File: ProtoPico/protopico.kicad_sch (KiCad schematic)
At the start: 35 parts, among them J1 Screw_Terminal_01x02, J2 Backpack, J3 Other Fin, J4 BoopSensor, J5 Badger, J6 Face Power, J7 Face Matrices, M1 Fan, U1 Pimoroni_TinyRP2040, U2 Pololu D36V28F5, U3 Pololu D24V10F3, U4 74LS125

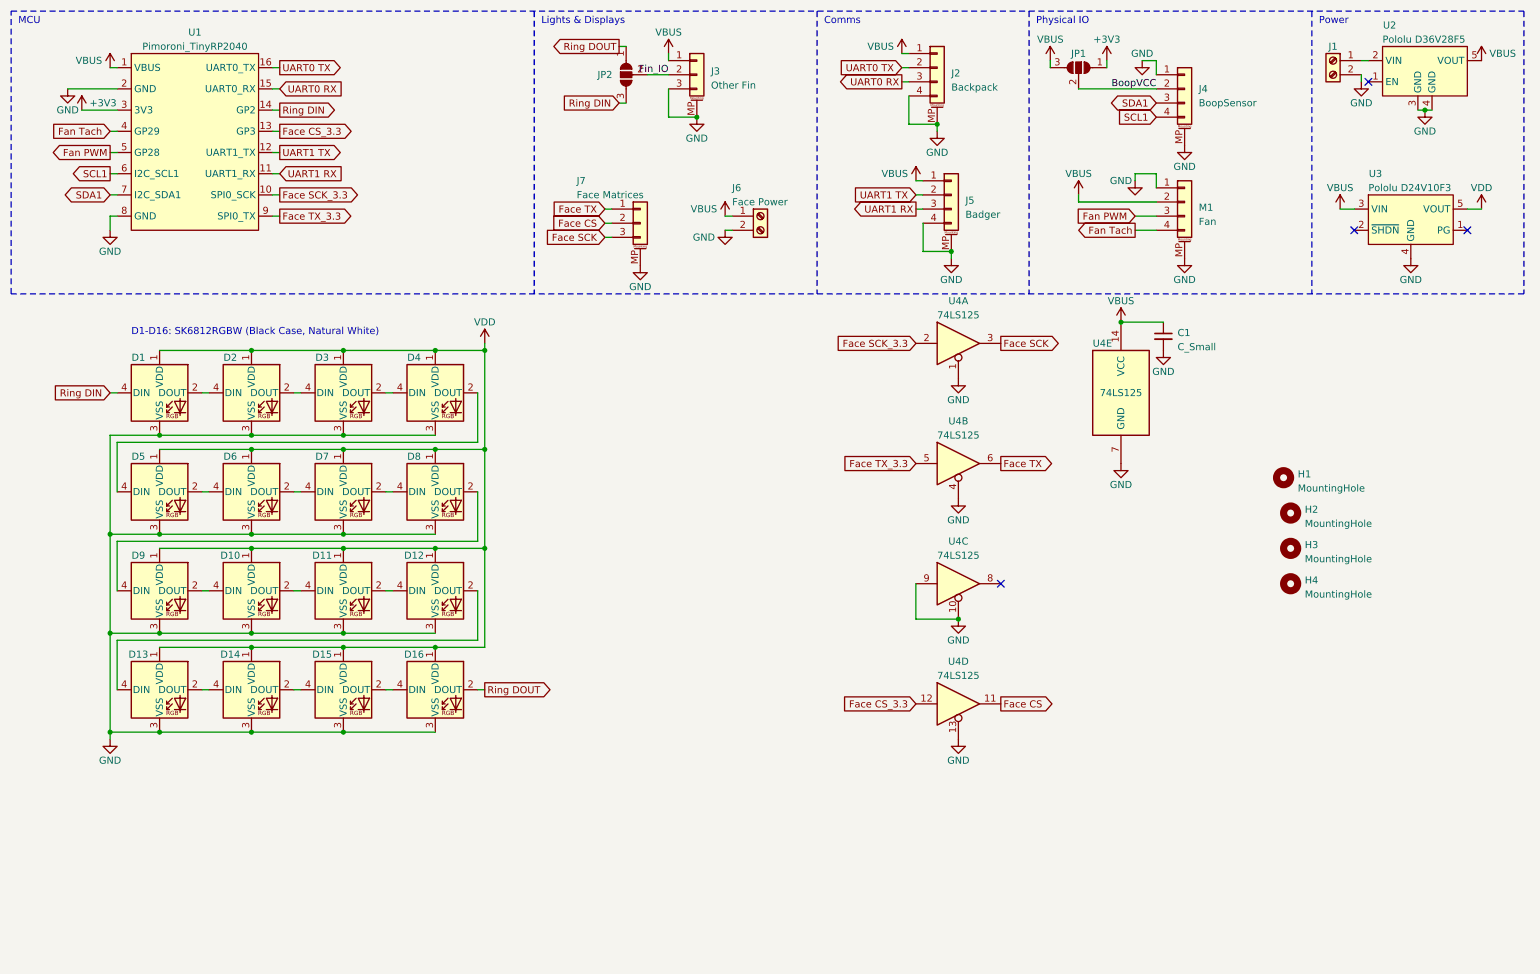
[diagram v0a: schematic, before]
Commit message: Update cheek pcb to Rev 2
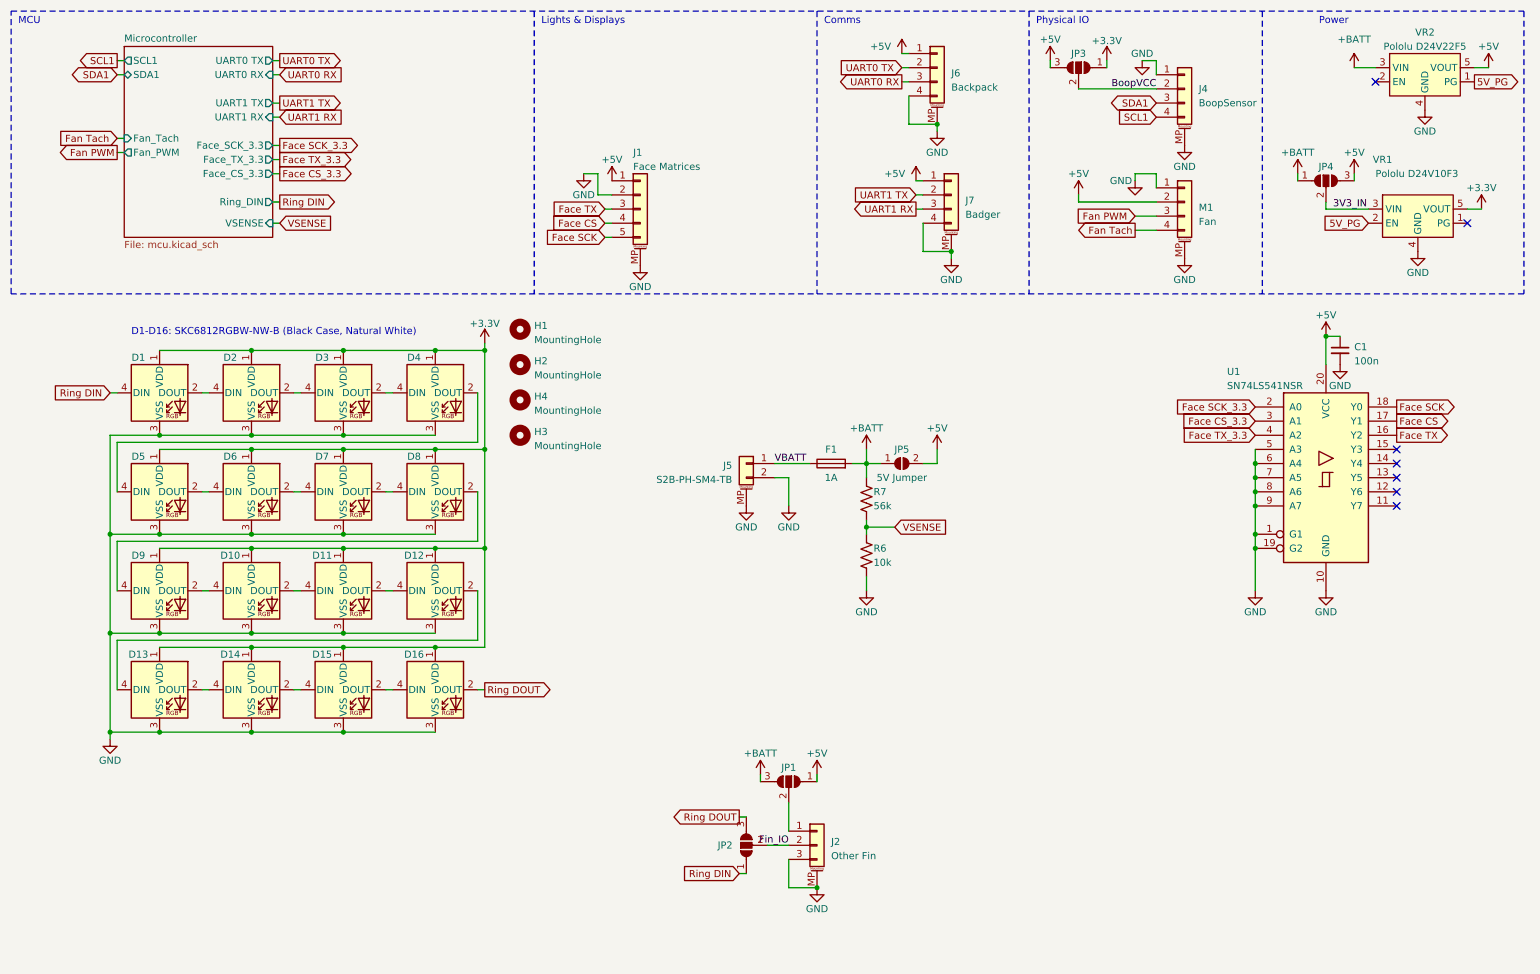
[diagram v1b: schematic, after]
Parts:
- removed J1: Screw_Terminal_01x02, TerminalBlock:TerminalBlock_bornier-2_P5.08mm, symbol Connector:Screw_Terminal_01x02
- removed J3: Other Fin, Connector_JST:JST_PH_S3B-PH-SM4-TB_1x03-1MP_P2.00mm_Horizontal, symbol Connector_Generic_MountingPin:Conn_01x03_MountingPin
- removed J6: Face Power, TerminalBlock:TerminalBlock_bornier-2_P5.08mm, symbol Connector:Screw_Terminal_01x02
- removed J7: Face Matrices, Connector_JST:JST_GH_SM03B-GHS-TB_1x03-1MP_P1.25mm_Horizontal, symbol Connector_Generic_MountingPin:Conn_01x03_MountingPin
- removed U1: Pimoroni_TinyRP2040, MCU_RaspberryPi_and_Boards:Pimoroni_TinyRP2040, symbol MCU_RaspberryPi_and_Boards:Pimoroni_TinyRP2040
- removed U2: Pololu D36V28F5, MyloLibrary:Pololu D36V28Fx, symbol New_Library:Pololu D36V28F5
- removed U4: 74LS125, Package_SO:TSSOP-14_4.4x5mm_P0.65mm, symbol 74xx:74LS125
- added F1: 1A, Fuse:Fuse_1206_3216Metric, symbol Device:Fuse
- added J1: Face Matrices, ProtoPico_Footprints:JST_SH_SM05B-SRSS-TB_1x05-1MP_P1.00mm_Horizontal, symbol Connector_Generic_MountingPin:Conn_01x05_MountingPin
- added J2: Other Fin, Connector_JST:JST_PH_S3B-PH-SM4-TB_1x03-1MP_P2.00mm_Horizontal, symbol Connector_Generic_MountingPin:Conn_01x03_MountingPin
- added J5: S2B-PH-SM4-TB, Connector_JST:JST_PH_S2B-PH-SM4-TB_1x02-1MP_P2.00mm_Horizontal, symbol Connector_Generic_MountingPin:Conn_01x02_MountingPin
- added JP1, JP4: SolderJumper_3_Open, Jumper:SolderJumper-3_P2.0mm_Open_TrianglePad1.0x1.5mm_NumberLabels, symbol Jumper:SolderJumper_3_Open
- added JP5: 5V Jumper, Jumper:SolderJumper-2_P1.3mm_Open_TrianglePad1.0x1.5mm, symbol Jumper:SolderJumper_2_Open
- added R6: 10k, Resistor_SMD:R_0805_2012Metric, symbol Device:R_US
- added R7: 56k, Resistor_SMD:R_0805_2012Metric, symbol Device:R_US
- added U1: SN74LS541NSR, Package_SO:SO-20_5.3x12.6mm_P1.27mm, symbol 74xx:74LS541
- added VR2: Pololu D24V22F5, ProtoPico_Footprints:D24V22FX, symbol ProtoPico_Symbols:D24V22Fx
- C1: value C_Small -> 100n
- D1, D10, D11, D12, D13, D14, D15, D16, D2, D3, D4, D5, D6, D7, D8, D9: value SK6812RGBW -> SKC6812RGBW-NW-B
- J4, M1: footprint Connector_JST:JST_GH_SM04B-GHS-TB_1x04-1MP_P1.25mm_Horizontal -> ProtoPico_Footprints:JST_SH_SM04B-SRSS-TB_1x04-1MP_P1.00mm_Horizontal
- J6: renamed from J2; footprint Connector_JST:JST_GH_SM04B-GHS-TB_1x04-1MP_P1.25mm_Horizontal -> ProtoPico_Footprints:JST_SH_SM04B-SRSS-TB_1x04-1MP_P1.00mm_Horizontal
- J7: renamed from J5; footprint Connector_JST:JST_GH_SM04B-GHS-TB_1x04-1MP_P1.25mm_Horizontal -> ProtoPico_Footprints:JST_SH_SM04B-SRSS-TB_1x04-1MP_P1.00mm_Horizontal
- VR1: renamed from U3; footprint MyloLibrary:Pololu D24V10Fx -> ProtoPico_Footprints:D24V10Fx; symbol New_Library:Pololu D24V10F3 -> ProtoPico_Symbols:D24V10Fx
- renumbered H4 to H3, H3 to H4, JP1 to JP3
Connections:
- net VDD is gone; now on net +3.3V: D1.1 (VDD), D10.1 (VDD), D11.1 (VDD), D12.1 (VDD), D13.1 (VDD), D14.1 (VDD), D15.1 (VDD), D16.1 (VDD), D2.1 (VDD), D3.1 (VDD), D4.1 (VDD), D5.1 (VDD), D6.1 (VDD), D7.1 (VDD), D8.1 (VDD), D9.1 (VDD), VR1.5 (VOUT)
- net Face CS: now also J1.4 (Pin_4), U1.17 (Y1)
- net Face CS_3.3: now also U1.3 (A1)
- net Face SCK: now also J1.5 (Pin_5), U1.18 (Y0)
- net Face SCK_3.3: now also U1.2 (A0)
- net Face TX: now also J1.3 (Pin_3), U1.16 (Y2)
- net Face TX_3.3: now also U1.4 (A2)
- net Fin_IO: now also J2.2 (Pin_2)
- net GND: now also J1.2 (Pin_2), J1.MP (MountPin), J2.3 (Pin_3), J2.MP (MountPin), J5.2 (Pin_2), J5.MP (MountPin), R6.2, U1.1 (G1), U1.10 (GND), U1.19 (G2), U1.5 (A3), U1.6 (A4), U1.7 (A5), U1.8 (A6), U1.9 (A7), VR2.4 (GND), VR2.6 (GND)
- net Ring DIN: now also JP2.1 (A); no longer JP2.3 (B)
- net Ring DOUT: now also JP2.3 (B); no longer JP2.1 (A)
- net 5V_PG: now reaches VR1.2 (EN)
- net 5V_PG: now also VR2.1 (PG)
- net +3V3 renamed +3.3V
- net VBUS renamed +5V
- net +5V: now also J1.1 (Pin_1), JP1.1 (A), JP4.3 (B), JP5.2 (B), U1.20 (VCC), VR2.5 (VOUT); no longer VR1.3 (VIN)
- new net: J2.1 (Pin_1), JP1.2 (C)
- new net +BATT: F1.2, JP1.3 (B), JP4.1 (A), JP5.1 (A), R7.1, VR2.3 (VIN)
- new net 3V3_IN: JP4.2 (C), VR1.3 (VIN)
- new net VBATT: F1.1, J5.1 (Pin_1)
- new net VSENSE: R6.1, R7.2
- no-connect marks 4 -> 7
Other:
- added sheet Microcontroller (mcu.kicad_sch)
- note added: "D1-D16: SKC6812RGBW-NW-B (Black Case, Natural White)"
- note removed: "D1-D16: SK6812RGBW (Black Case, Natural White)"
- moved on the sheet: C1, H1, H2, H3, H4, VR1

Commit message: Update to V2 of Backpack
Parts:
- removed H3, H4: MountingHole, MountingHole:MountingHole_3.2mm_M3, symbol Mechanical:MountingHole
- removed JP1, JP2, JP3, JP4: SolderJumper_3_Open, Jumper:SolderJumper-3_P2.0mm_Open_TrianglePad1.0x1.5mm_NumberLabels, symbol Jumper:SolderJumper_3_Open
- removed JP5: 5V Jumper, Jumper:SolderJumper-2_P1.3mm_Open_TrianglePad1.0x1.5mm, symbol Jumper:SolderJumper_2_Open
- removed VR1: Pololu D24V10F3, ProtoPico_Footprints:D24V10Fx, symbol ProtoPico_Symbols:D24V10Fx
- removed VR2: Pololu D24V22F5, ProtoPico_Footprints:D24V22FX, symbol ProtoPico_Symbols:D24V22Fx
- added R3: 100, Resistor_SMD:R_0402_1005Metric, symbol Device:R_Small_US
- C1: footprint Capacitor_SMD:C_0805_2012Metric_Pad1.18x1.45mm_HandSolder -> Capacitor_SMD:C_0402_1005Metric
- F1: footprint Fuse:Fuse_1206_3216Metric -> Fuse:Fuse_1206_3216Metric_Pad1.42x1.75mm_HandSolder
- H1, H2: value MountingHole -> M3 Hole; footprint MountingHole:MountingHole_3.2mm_M3 -> MountingHole:MountingHole_3.2mm_M3_ISO14580; now left out of the parts list
- J1: renamed from J6; now not fitted; now left out of the parts list
- J2: renamed from J4; footprint ProtoPico_Footprints:JST_SH_SM04B-SRSS-TB_1x04-1MP_P1.00mm_Horizontal -> Connector_JST:JST_GH_SM04B-GHS-TB_1x04-1MP_P1.25mm_Horizontal
- J3: renamed from J7; now not fitted; now left out of the parts list
- J4: renamed from J1; value Face Matrices -> S5B-PH-SM4-TB; footprint ProtoPico_Footprints:JST_SH_SM05B-SRSS-TB_1x05-1MP_P1.00mm_Horizontal -> Connector_JST:JST_PH_S5B-PH-SM4-TB_1x05-1MP_P2.00mm_Horizontal
- J6: renamed from J2; value Other Fin -> S3B-PH-SM4-TB
- M1: footprint ProtoPico_Footprints:JST_SH_SM04B-SRSS-TB_1x04-1MP_P1.00mm_Horizontal -> Connector_JST:JST_GH_SM04B-GHS-TB_1x04-1MP_P1.25mm_Horizontal
- R1: renamed from R7; footprint Resistor_SMD:R_0805_2012Metric -> Resistor_SMD:R_0805_2012Metric_Pad1.20x1.40mm_HandSolder
- R2: renamed from R6; value 10k -> 12k; footprint Resistor_SMD:R_0805_2012Metric -> Resistor_SMD:R_0805_2012Metric_Pad1.20x1.40mm_HandSolder
- U1: footprint Package_SO:SO-20_5.3x12.6mm_P1.27mm -> Package_SO:TSSOP-20_4.4x6.5mm_P0.65mm
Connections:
- net BoopVCC is gone; now on net +3.3V: J2.2 (Pin_2)
- net Fin_IO is gone; now on net Ring DOUT: J6.2 (Pin_2)
- net +5V: now also J6.1 (Pin_1)
- net Face SCK: now also U1.16 (Y2); no longer U1.18 (Y0)
- net Face SCK_3.3: now also U1.4 (A2); no longer U1.2 (A0)
- net Face TX: now also U1.18 (Y0); no longer U1.16 (Y2)
- net Face TX_3.3: now also U1.2 (A0); no longer U1.4 (A2)
- net Ring DOUT: now also R3.2; no longer D16.2 (DOUT)
- new net: D16.2 (DOUT), R3.1
- no-connect marks 7 -> 5
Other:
- added sheet Voltage Regulators (reg_3v3.kicad_sch)
- sheet Microcontroller ports: added 5V_EN, 5V_PG; removed UART0 RX, UART0 TX, UART1 RX, UART1 TX
- note added: "D1-D16: SKC6812RGBW-NW-B (Natural White, Black Case)"
- note removed: "D1-D16: SKC6812RGBW-NW-B (Black Case, Natural White)"
- moved on the sheet: C1, H1, H2, J4, J6, U1
